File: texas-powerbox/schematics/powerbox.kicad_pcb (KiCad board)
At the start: 2 copper layers, 32 parts, among them J1 BATTERY, J2 ADAPTER, J3 USB_STACKED, J4 USB_STACKED, K1 J107F1CS1224VDC.36, Q1 AOD417, U1 TPS54331GDR

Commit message: routing
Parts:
- added REF**: MountingHole_3.2mm_M3_Pad, MountingHole:MountingHole_3.2mm_M3_Pad, F.Cu at (111.8, 95.2)
- added REF**: MountingHole_3.2mm_M3_Pad, MountingHole:MountingHole_3.2mm_M3_Pad, F.Cu at (111.8, 154.9)
- added REF**: MountingHole_3.2mm_M3_Pad, MountingHole:MountingHole_3.2mm_M3_Pad, F.Cu at (195.6, 154.9)
- added REF**: MountingHole_3.2mm_M3_Pad, MountingHole:MountingHole_3.2mm_M3_Pad, F.Cu at (195.6, 95.2)
- D1: value AUX -> EXT
- J7: value ~ -> 5V
- J8: value ~ -> 24V
- moved F2 66.9 mm to (165.6, 154.9), turned to 0 degrees
- moved J8 57.4 mm to (143.5, 102.2), turned to 0 degrees
- moved J7 57.0 mm to (123.8, 102.2), turned to 0 degrees
- moved F1 47.6 mm to (165.7, 144.8), turned to 0 degrees
- moved R6 41.8 mm to (135.6, 108.2), turned to 90 degrees
- moved D6 40.7 mm to (130.6, 108.2), turned to 90 degrees
- moved D3 20.7 mm to (164.5, 135.9), turned to 90 degrees
- moved D2 18.9 mm to (170.2, 135.9), turned to 90 degrees
- moved K1 16.2 mm to (165.7, 118.7), turned to 90 degrees
- moved C5 15.2 mm to (114.3, 115.9), turned to 90 degrees
- moved R2 13.4 mm to (157.2, 127.6), turned to 270 degrees
- moved C6 10.6 mm to (114.3, 108.2)
- moved R5 9.90 mm to (124.5, 108.2), turned to 90 degrees
- moved R3 9.84 mm to (119.4, 115.9), turned to 90 degrees
- moved R4 8.73 mm to (119.4, 108.2), turned to 270 degrees
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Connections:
- F1 pad 1: GND -> Net-(F1-Pad1)
- J1 pad 1: Net-(F1-Pad2) -> GND
- J2 pad 2: Net-(F1-Pad2) -> GND
- K1 pad 1: Net-(K1-Pad1) -> Net-(F1-Pad1)
- Q1 pad 2: Net-(K1-Pad1) -> Net-(F1-Pad2)
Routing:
- net +5V: track 0.00 -> 126.7 mm
- net Net-(C6-Pad1): track 0.00 -> 113.7 mm
- net Net-(D1-Pad2): track 0.00 -> 67.2 mm
- net +24V: track 0.00 -> 46.4 mm
- net Net-(F1-Pad1): track 0.00 -> 42.9 mm
- net Net-(D2-Pad2): track 0.00 -> 41.8 mm
- net Net-(C3-Pad1): track 0.00 -> 29.7 mm
- net Net-(J2-Pad1): track 0.00 -> 29.3 mm
- net Net-(J1-Pad2): track 0.00 -> 23.0 mm
- net Net-(K1-Pad4): track 0.00 -> 20.6 mm
- net Net-(F1-Pad2): track 0.00 -> 17.0 mm
- net Net-(R4-Pad2): track 0.00 -> 17.0 mm
- net Net-(C4-Pad1): track 0.00 -> 16.1 mm
- net Net-(D4-Pad2): track 0.00 -> 9.38 mm
- net Net-(C2-Pad1): track 0.00 -> 8.29 mm
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- added copper zone on F.Cu, net GND
- removed copper zone on B.Cu, net (none)
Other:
- board outline added: 94 x 68.6 mm

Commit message: Fix pr issues and add logo
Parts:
- added G***: LOGO, Team_Logo:Logo_SilkScreen_10mm, F.Cu at (154.4, 110.0)
- moved C1 2.67 mm to (140.2, 121.4)
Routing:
- net +24V: track 46.4 -> 50.7 mm
- net +5V: track 126.7 -> 129.5 mm
- net GND: track 7.01 -> 5.11 mm
- net Net-(D1-Pad2): track 67.2 -> 65.7 mm
- net Net-(F1-Pad1): track 42.9 -> 43.7 mm
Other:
- net class Default removed
- board text added: "Rio Liu Waterloo Rocketry"

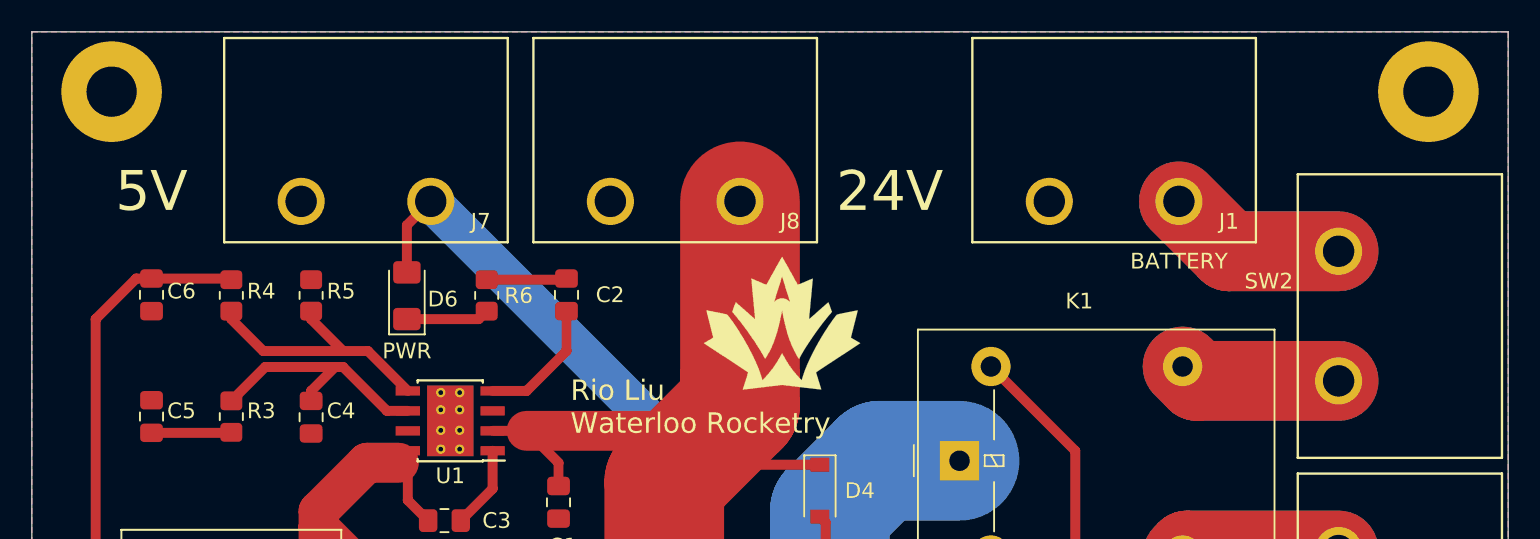
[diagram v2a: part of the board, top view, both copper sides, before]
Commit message: align mounting holes and name the board
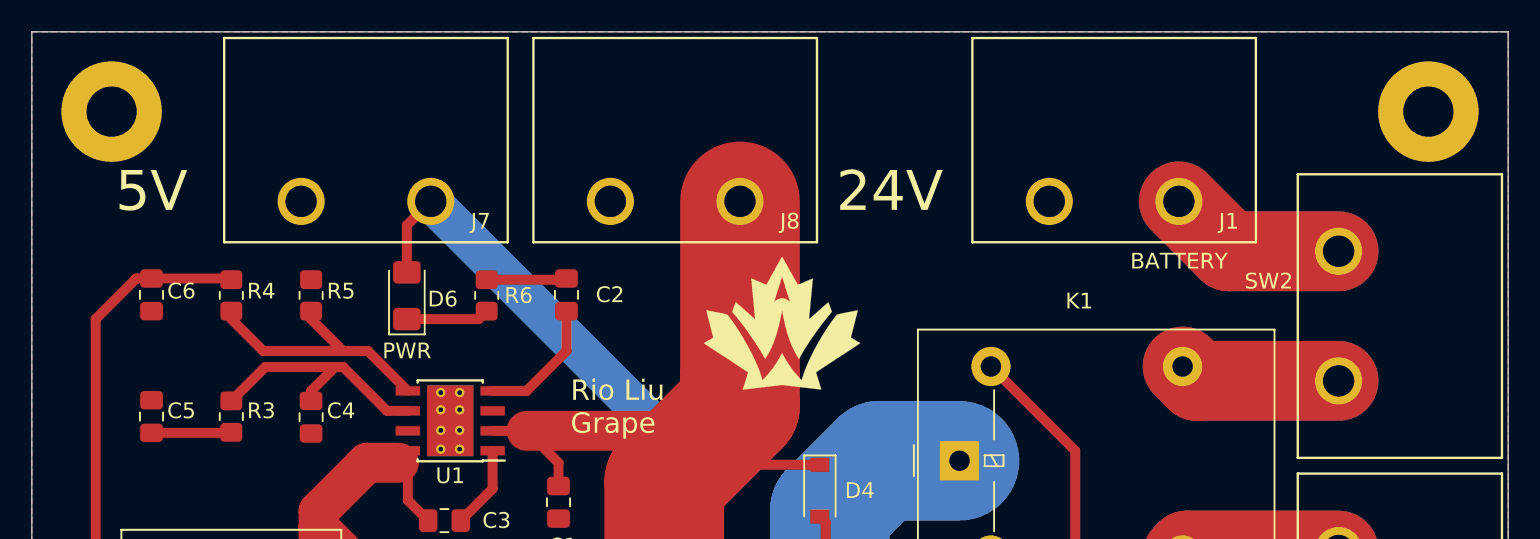
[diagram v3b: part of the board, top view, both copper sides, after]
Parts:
- moved REF** 1.27 mm to (195.6, 96.5)
- moved REF** 1.27 mm to (111.8, 96.5)
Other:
- board text added: "Rio Liu Grape"
- board text removed: "Rio Liu Waterloo Rocketry"
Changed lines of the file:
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@@
   )
   (footprint "MountingHole:MountingHole_3.2mm_M3_Pad" (layer "F.Cu")
-    (at 195.58 95.25)
+    (at 195.58 96.52)
     (descr "Mounting Hole 3.2mm, M3")
     (tags "mounting hole 3.2mm m3")
@@
   )
   (footprint "MountingHole:MountingHole_3.2mm_M3_Pad" (layer "F.Cu")
-    (at 111.76 95.25)
+    (at 111.76 96.52)
     (descr "Mounting Hole 3.2mm, M3")
     (tags "mounting hole 3.2mm m3")
@@
   (gr_line (start 200.66 91.44) (end 200.66 160.02) (layer "Edge.Cuts") (width 0.05))
   (gr_line (start 200.66 160.02) (end 106.68 160.02) (layer "Edge.Cuts") (width 0.05))
-  (gr_text "Rio Liu\nWaterloo Rocketry" (at 140.97 115.316) (layer "F.SilkS")
+  (gr_text "Rio Liu\nGrape" (at 140.97 115.316) (layer "F.SilkS")
     (effects (font (size 1.3 1.3) (thickness 0.3)) (justify left))
   )

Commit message: project cleanup
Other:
- board text added: "Rio Liu Grape V2 2022-01-23"
- board text removed: "Rio Liu Grape"
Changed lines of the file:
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@@
   (gr_line (start 200.66 91.44) (end 200.66 160.02) (layer "Edge.Cuts") (width 0.05))
   (gr_line (start 200.66 160.02) (end 106.68 160.02) (layer "Edge.Cuts") (width 0.05))
-  (gr_text "Rio Liu\nGrape" (at 140.97 115.316) (layer "F.SilkS")
+  (gr_text "Rio Liu\nGrape V2\n2022-01-23" (at 140.97 115.316) (layer "F.SilkS")
     (effects (font (size 1.3 1.3) (thickness 0.3)) (justify left))
+  )
+  (dimension (type aligned) (layer "Dwgs.User")
+    (pts (xy 111.76 96.52) (xy 111.76 91.44))
+    (height -15.24)
+    (gr_text "5.08 mm" (at 95.37 93.98 90) (layer "Dwgs.User")
+      (effects (font (size 1 1) (thickness 0.15)))
+    )
+    (format (units 3) (units_format 1) (precision 2))
+    (style (thickness 0.1) (arrow_length 1.27) (text_position_mode 0) (extension_height 0.58642) (extension_offset 0.5) keep_text_aligned)
+  )
+  (dimension (type aligned) (layer "Dwgs.User")
+    (pts (xy 111.76 96.52) (xy 111.76 154.94))
+    (height 15.239999)
+    (gr_text "58.42 mm" (at 95.370001 125.73 90) (layer "Dwgs.User")
+      (effects (font (size 1 1) (thickness 0.15)))
+    )
+    (format (units 3) (units_format 1) (precision 2))
+    (style (thickness 0.1) (arrow_length 1.27) (text_position_mode 0) (extension_height 0.58642) (extension_offset 0.5) keep_text_aligned)
+  )
+  (dimension (type aligned) (layer "Dwgs.User")
+    (pts (xy 106.68 160.02) (xy 106.68 91.44))
+    (height -21.59)
+    (gr_text "68.58 mm" (at 83.94 125.73 90) (layer "Dwgs.User")
+      (effects (font (size 1 1) (thickness 0.15)))
+    )
+    (format (units 3) (units_format 1) (precision 2))
+    (style (thickness 0.1) (arrow_length 1.27) (text_position_mode 0) (extension_height 0.58642) (extension_offset 0.5) keep_text_aligned)
+  )
+  (dimension (type aligned) (layer "Dwgs.User")
+    (pts (xy 106.68 91.44) (xy 200.66 91.44))
+    (height -13.97)
+    (gr_text "93.98 mm" (at 153.67 76.32) (layer "Dwgs.User")
+      (effects (font (size 1 1) (thickness 0.15)))
+    )
+    (format (units 3) (units_format 1) (precision 2))
+    (style (thickness 0.1) (arrow_length 1.27) (text_position_mode 0) (extension_height 0.58642) (extension_offset 0.5) keep_text_aligned)
+  )
+  (dimension (type aligned) (layer "Dwgs.User")
+    (pts (xy 195.58 96.52) (xy 111.76 96.52))
+    (height 11.429999)
+    (gr_text "83.82 mm" (at 153.67 83.940001) (layer "Dwgs.User")
+      (effects (font (size 1 1) (thickness 0.15)))
+    )
+    (format (units 3) (units_format 1) (precision 2))
+    (style (thickness 0.1) (arrow_length 1.27) (text_position_mode 0) (extension_height 0.58642) (extension_offset 0.5) keep_text_aligned)
   )
   (segment (start 140.641 107.22) (end 140.716 107.145) (width 0.635) (layer "F.Cu") (net 1))
@@
       )
     )
-  )
-  (zone (net 0) (net_name "") (layer "F.Mask") (hatch edge 0.508)
-    (connect_pads (clearance 0.508))
-    (min_thickness 0.254) (filled_areas_thickness no)
-    (fill yes (thermal_gap 0.508) (thermal_bridge_width 0.508))
-    (polygon
-      (pts
-        (xy 138.2776 117.1448)
-        (xy 135.2423 117.1448)
-        (xy 135.2423 116.5352)
-        (xy 138.2776 116.5352)
-      )
-    )
-  )
-  (zone (net 0) (net_name "") (layer "F.Mask") (hatch edge 0.508)
-    (connect_pads (clearance 0.508))
-    (min_thickness 0.254) (filled_areas_thickness no)
-    (fill yes (thermal_gap 0.508) (thermal_bridge_width 0.508))
-    (polygon
-      (pts
-        (xy 131.3815 118.4275)
-        (xy 128.4605 118.4275)
-        (xy 128.4605 117.7925)
-        (xy 131.3815 117.7925)
-      )
-    )

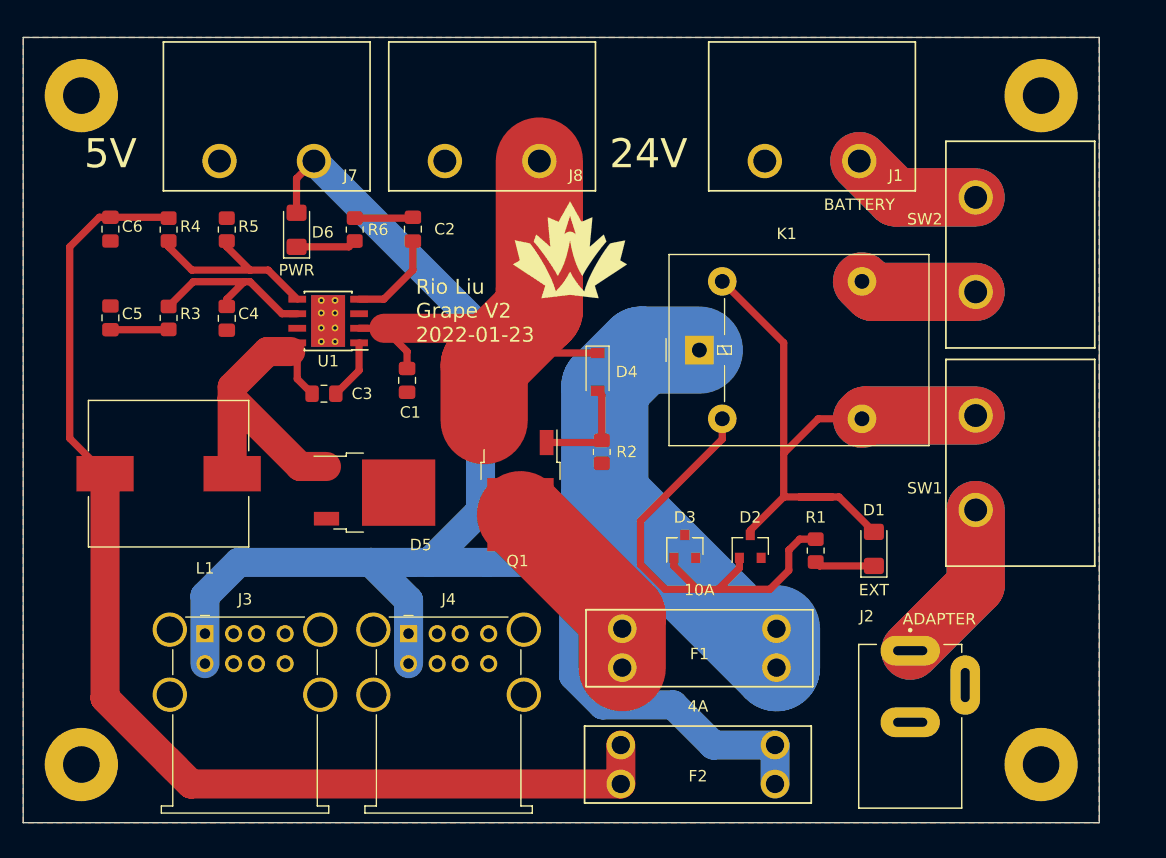
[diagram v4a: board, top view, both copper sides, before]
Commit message: updated to use alternative bulk converter
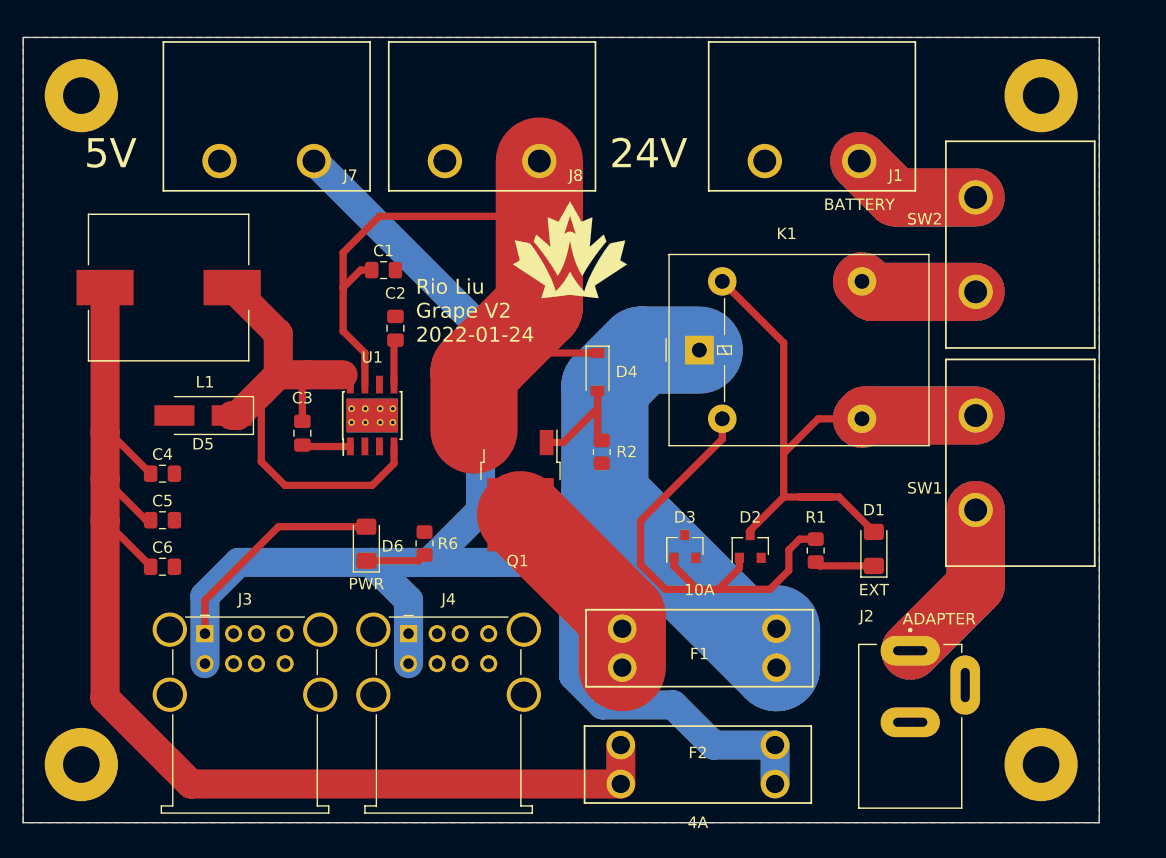
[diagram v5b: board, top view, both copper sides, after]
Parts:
- removed R3: 64.9k, Resistor_SMD:R_0805_2012Metric_Pad1.20x1.40mm_HandSolder
- removed R4: 10.2k, Resistor_SMD:R_0805_2012Metric_Pad1.20x1.40mm_HandSolder
- removed R5: 1.96k, Resistor_SMD:R_0805_2012Metric_Pad1.20x1.40mm_HandSolder
- C1: value 10uF -> 1uF
- C2: value 8.2nF -> 0.39uF
- C3: value 0.1uF -> 10nF
- C4: value 10pF -> 47uF
- C5: value 1nF -> 10uF
- C6: value 47uF -> 2.2uF
- D5: value FERD15S50S -> SK510ATR; footprint Package_TO_SOT_SMD:TO-252-2 -> Diode_SMD:D_SMA_Handsoldering
- U1: value TPS54331GDR -> LM22673-5.0
- moved C6 29.8 mm to (118.9, 137.7), turned to 0 degrees
- moved R6 28.1 mm to (141.7, 135.6)
- moved D6 28.1 mm to (136.7, 135.7)
- moved C5 18.3 mm to (118.9, 133.6), turned to 0 degrees
- moved D5 16.4 mm to (122.4, 124.5), turned to 180 degrees
- moved L1 16.3 mm to (119.4, 113.3)
- moved C4 14.7 mm to (118.9, 129.5), turned to 0 degrees
- moved C1 9.85 mm to (138.2, 111.8), turned to 0 degrees
- moved U1 9.11 mm to (137.2, 124.5), turned to 90 degrees
- moved C2 8.79 mm to (139.2, 116.8)
- moved C3 3.93 mm to (131.1, 126.0), turned to 90 degrees
- turned F2 to 180 degrees
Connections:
- C2 pad 1: Net-(C2-Pad1) -> Net-(U1-Pad5)
- C3 pad 1: Net-(C3-Pad1) -> Net-(U1-Pad1)
- C3 pad 2: Net-(C3-Pad2) -> Net-(D5-Pad1)
- C4 pad 1: Net-(C4-Pad1) -> Net-(L1-Pad2)
- C5 pad 1: Net-(C5-Pad1) -> Net-(L1-Pad2)
- C6 pad 1: Net-(C6-Pad1) -> Net-(L1-Pad2)
- D5 pad 1: Net-(C3-Pad1) -> Net-(D5-Pad1)
- F2 pad 1: +5V -> Net-(L1-Pad2)
- F2 pad 2: Net-(C6-Pad1) -> +5V
- J3 pad 2: (no net) -> unconnected-(J3-Pad2)
- J3 pad 3: (no net) -> unconnected-(J3-Pad3)
- J3 pad 6: (no net) -> unconnected-(J3-Pad6)
- J3 pad 7: (no net) -> unconnected-(J3-Pad7)
- J4 pad 2: (no net) -> unconnected-(J4-Pad2)
- J4 pad 3: (no net) -> unconnected-(J4-Pad3)
- J4 pad 6: (no net) -> unconnected-(J4-Pad6)
- J4 pad 7: (no net) -> unconnected-(J4-Pad7)
- L1 pad 1: Net-(C3-Pad1) -> Net-(D5-Pad1)
- L1 pad 2: Net-(C6-Pad1) -> Net-(L1-Pad2)
- U1 pad 1: Net-(C3-Pad2) -> Net-(U1-Pad1)
- U1 pad 2: +24V -> unconnected-(U1-Pad2)
- U1 pad 3: (no net) -> unconnected-(U1-Pad3)
- U1 pad 4: Net-(C2-Pad1) -> Net-(D5-Pad1)
- U1 pad 5: Net-(R4-Pad2) -> Net-(U1-Pad5)
- U1 pad 6: Net-(C4-Pad1) -> GND
- U1 pad 7: GND -> +24V
- U1 pad 8: Net-(C3-Pad1) -> Net-(D5-Pad1)
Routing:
- net Net-(L1-Pad2): track 0.00 -> 115.8 mm
- net Net-(C6-Pad1): track 113.7 -> 0.00 mm
- net Net-(D5-Pad1): track 0.00 -> 47.5 mm
- net Net-(C3-Pad1): track 29.7 -> 0.00 mm
- net +24V: track 50.7 -> 68.4 mm
- net Net-(R4-Pad2): track 17.0 -> 0.00 mm
- net Net-(C4-Pad1): track 16.1 -> 0.00 mm
- net +5V: track 129.5 -> 144.1 mm
- net Net-(C2-Pad1): track 8.29 -> 0.00 mm
- net Net-(C3-Pad2): track 5.29 -> 0.00 mm
- net GND: track 5.11 -> 0.00 mm
- net Net-(C5-Pad1): track 5.09 -> 0.00 mm
- net Net-(U1-Pad1): track 0.00 -> 4.51 mm
- net Net-(U1-Pad5): track 0.00 -> 3.94 mm
- net Net-(D4-Pad2): track 9.38 -> 10.4 mm
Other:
- board text added: "Rio Liu Grape V2 2022-01-24"
- board text removed: "Rio Liu Grape V2 2022-01-23"

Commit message: update regulator input capacitor and add comment
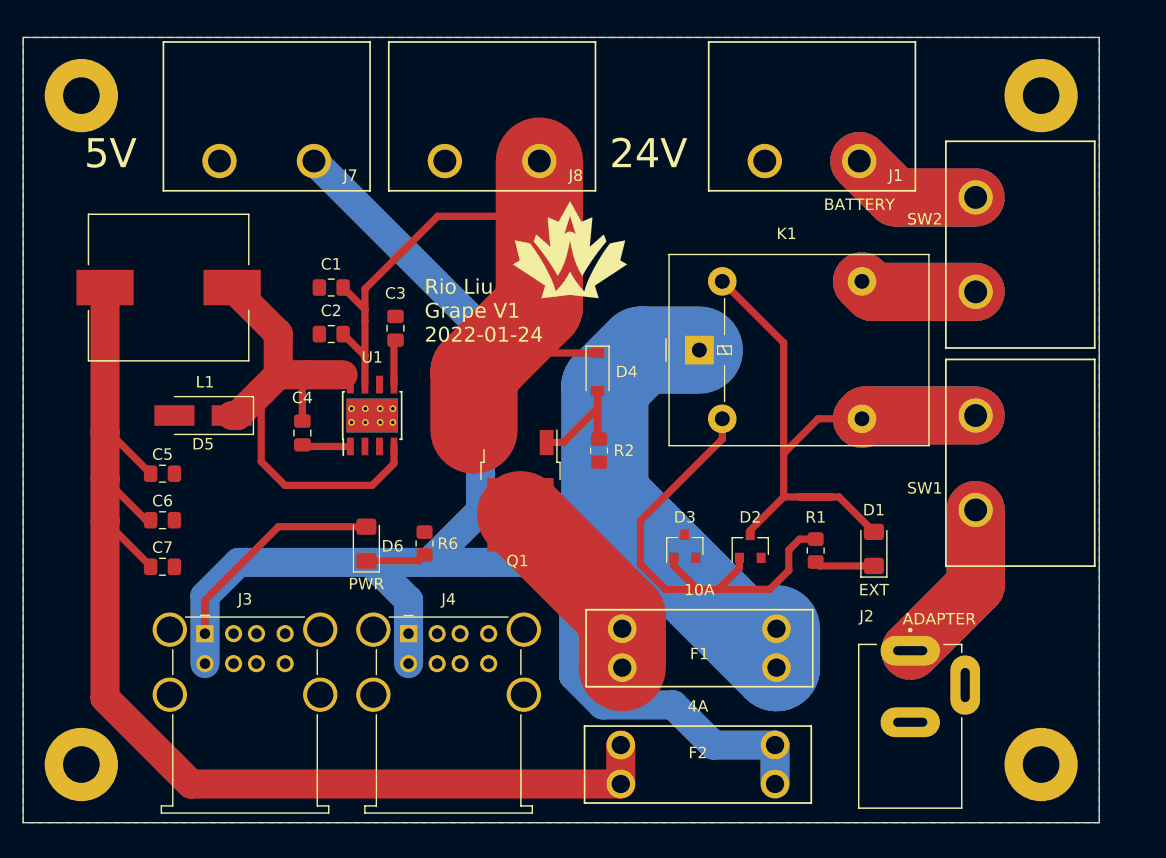
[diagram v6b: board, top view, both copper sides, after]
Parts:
- added C2: 1uF, Capacitor_SMD:C_0805_2012Metric_Pad1.18x1.45mm_HandSolder, F.Cu at (133.6, 117.3)
- C1: value 1uF -> 47uF
- moved C1 4.82 mm to (133.6, 113.3), turned to 180 degrees
- moved R2 0.26 mm to (157.0, 127.5)
- renumbered C2 to C3, C3 to C4, C4 to C5, C5 to C6, C6 to C7
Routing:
- net +24V: track 68.4 -> 66.1 mm
- net Net-(D4-Pad2): track 10.4 -> 9.66 mm
- net Net-(C4-Pad2): track 47.5 -> 46.7 mm
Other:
- board text added: "Rio Liu Grape V1 2022-01-24"
- board text removed: "Rio Liu Grape V2 2022-01-24"
